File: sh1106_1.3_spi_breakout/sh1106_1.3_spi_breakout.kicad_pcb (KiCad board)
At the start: 2 copper layers, 35 x 31 mm, 20 parts, among them J1 OLED_HEADER, J2 OLED_PANEL, Q1 Q_PMOS_GSD

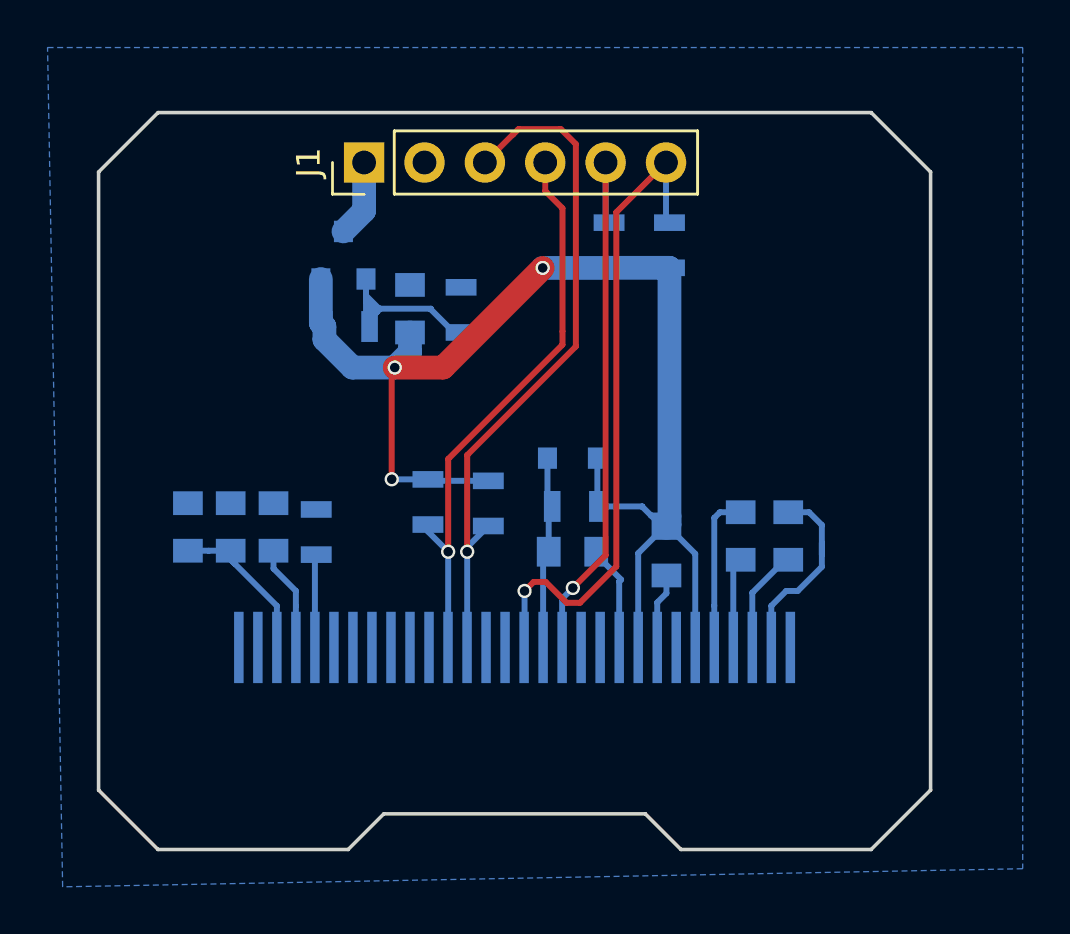
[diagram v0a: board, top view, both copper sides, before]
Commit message: Adjusted dimensions, added silkscreen markings
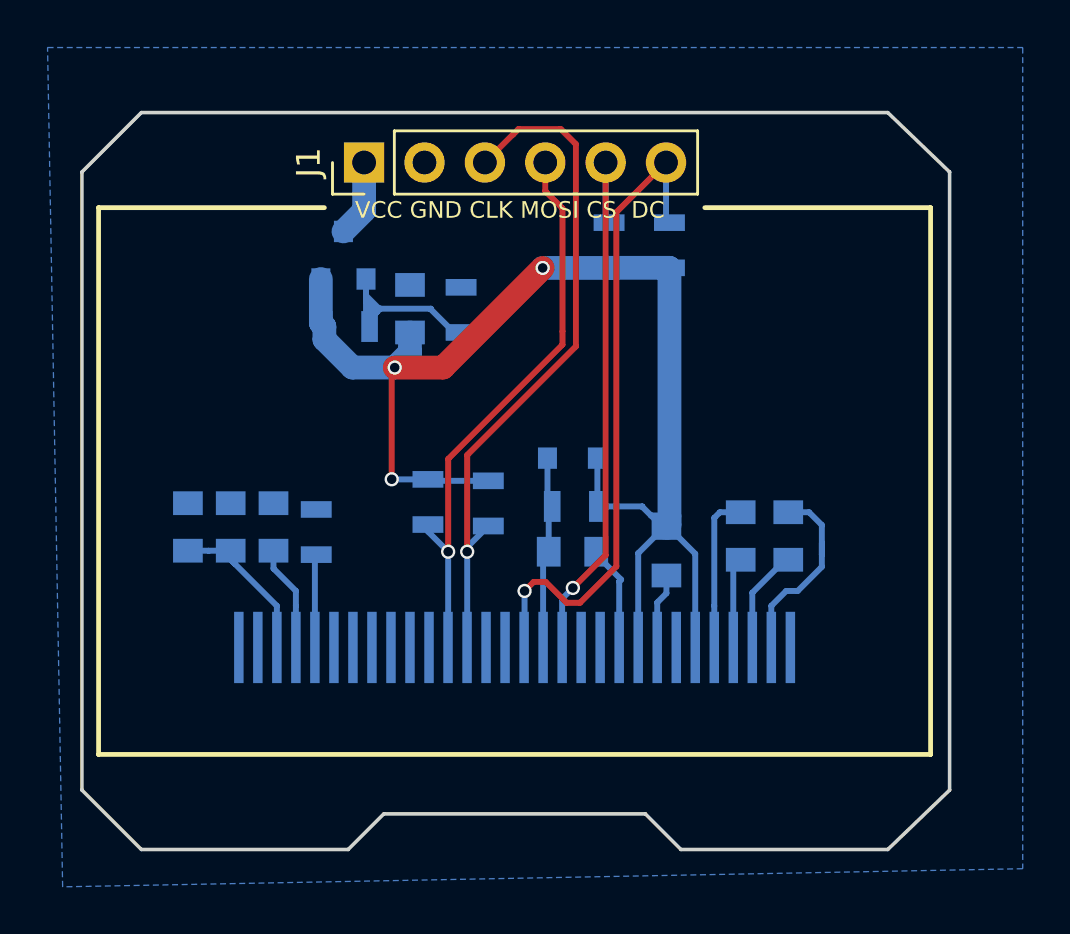
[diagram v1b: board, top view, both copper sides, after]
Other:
- board size 35 x 31 mm -> 36.5 x 31 mm
- board text added: "VCC GND CLK MOSI CS DC"
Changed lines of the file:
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@@
   (general
     (links 57)
-    (no_connects 57)
-    (area 32.424999 19.424999 67.575001 50.575001)
+    (no_connects 15)
+    (area 30.353 16.280952 71.374001 52.070001)
     (thickness 1.6)
-    (drawings 12)
+    (drawings 18)
     (tracks 149)
     (zones 0)
@@
     (pad_to_mask_clearance 0.2)
     (aux_axis_origin 0 0)
-    (visible_elements FFFFFF7F)
+    (visible_elements 7FFFFFFF)
     (pcbplotparams
       (layerselection 0x00030_80000001)
@@
       (zone_connect 1))
   )
+  (gr_text "VCC GND CLK MOSI CS  DC" (at 49.8 23.6) (layer F.SilkS)
+    (effects (font (size 0.7 0.7) (thickness 0.175)))
+  )
+  (gr_line (start 32.5 23.5) (end 42 23.5) (layer F.SilkS) (width 0.2))
+  (gr_line (start 58 23.5) (end 67.5 23.5) (layer F.SilkS) (width 0.2))
+  (gr_line (start 32.5 46.5) (end 32.5 23.5) (layer F.SilkS) (width 0.2))
+  (gr_line (start 67.5 46.5) (end 32.5 46.5) (layer F.SilkS) (width 0.2))
+  (gr_line (start 67.5 23.5) (end 67.5 46.5) (layer F.SilkS) (width 0.2))
   (gr_line (start 44.5 49) (end 43 50.5) (layer Edge.Cuts) (width 0.15))
   (gr_line (start 55.5 49) (end 44.5 49) (layer Edge.Cuts) (width 0.15))
   (gr_line (start 57 50.5) (end 55.5 49) (layer Edge.Cuts) (width 0.15))
-  (gr_line (start 65 50.5) (end 57 50.5) (layer Edge.Cuts) (width 0.15))
-  (gr_line (start 35 50.5) (end 43 50.5) (layer Edge.Cuts) (width 0.15))
-  (gr_line (start 32.5 48) (end 35 50.5) (layer Edge.Cuts) (width 0.15))
-  (gr_line (start 32.5 22) (end 32.5 48) (layer Edge.Cuts) (width 0.15))
-  (gr_line (start 35 19.5) (end 32.5 22) (layer Edge.Cuts) (width 0.15))
-  (gr_line (start 67.5 48) (end 65 50.5) (layer Edge.Cuts) (width 0.15))
-  (gr_line (start 67.5 22) (end 67.5 48) (layer Edge.Cuts) (width 0.15))
-  (gr_line (start 65 19.5) (end 67.5 22) (layer Edge.Cuts) (width 0.15))
-  (gr_line (start 35 19.5) (end 65 19.5) (layer Edge.Cuts) (width 0.15))
+  (gr_line (start 65.7 50.5) (end 57 50.5) (layer Edge.Cuts) (width 0.15))
+  (gr_line (start 34.3 50.5) (end 43 50.5) (layer Edge.Cuts) (width 0.15))
+  (gr_line (start 31.8 48) (end 34.3 50.5) (layer Edge.Cuts) (width 0.15))
+  (gr_line (start 31.8 22) (end 31.8 48) (layer Edge.Cuts) (width 0.15))
+  (gr_line (start 34.3 19.5) (end 31.8 22) (layer Edge.Cuts) (width 0.15))
+  (gr_line (start 68.3 48) (end 65.7 50.5) (layer Edge.Cuts) (width 0.15))
+  (gr_line (start 68.3 22) (end 68.3 48) (layer Edge.Cuts) (width 0.15))
+  (gr_line (start 65.7 19.5) (end 68.3 22) (layer Edge.Cuts) (width 0.15))
+  (gr_line (start 34.3 19.5) (end 65.7 19.5) (layer Edge.Cuts) (width 0.15))
   (segment (start 51.435 37.973) (end 51.435 36.216) (width 0.25) (layer B.Cu) (net 1))
   (segment (start 51.435 36.216) (end 51.583 36.068) (width 0.25) (layer B.Cu) (net 1))

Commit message: Small routing adjustments
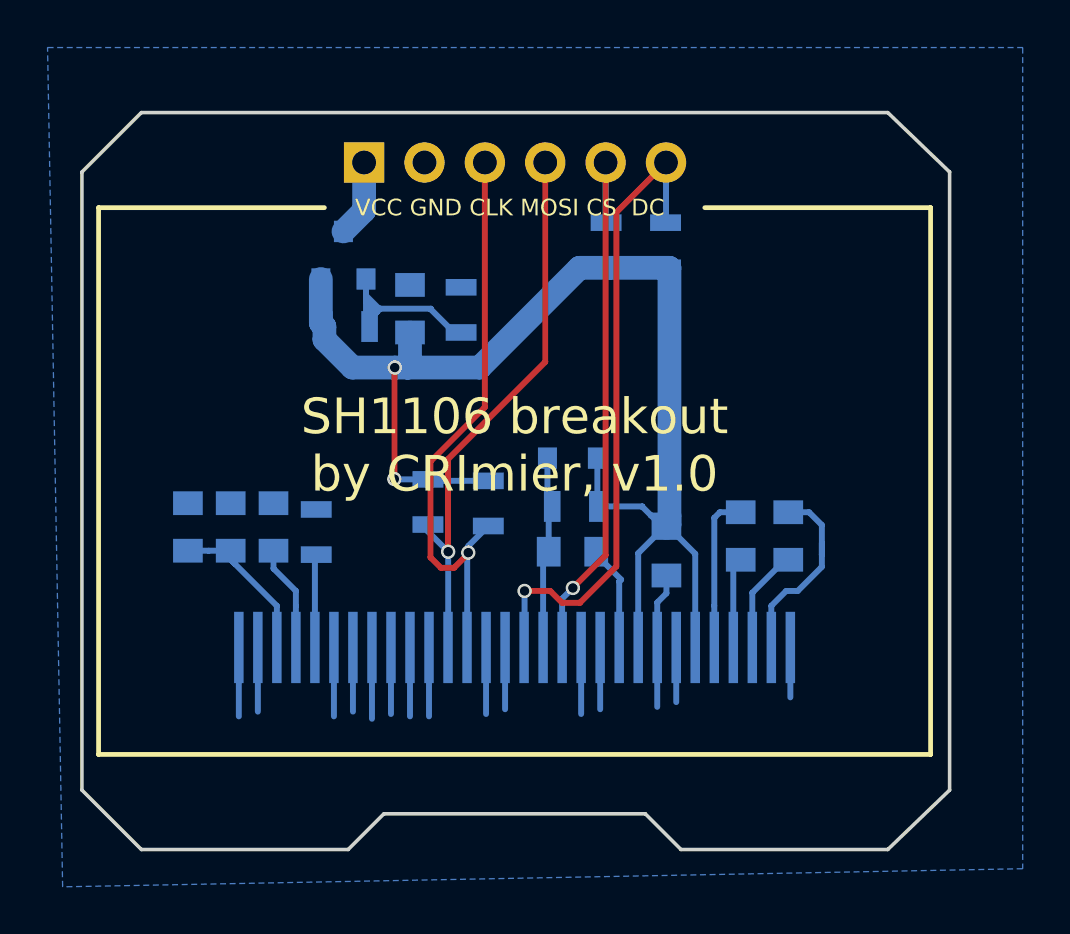
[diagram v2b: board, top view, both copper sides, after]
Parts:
- J1: moved to B.Cu
- moved R1 0.16 mm to (56.4, 25.1)
- moved R4 0.12 mm to (53.9, 25.1)
- turned J1 to 270 degrees
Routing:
- net GND: track 7.68 -> 48.2 mm
- net CLK: track 29.2 -> 25.1 mm
- net MOSI: track 24.2 -> 23.6 mm
- net +3V3: track 58.1 -> 57.6 mm, vias 3 -> 2
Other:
- board text added: "SH1106 breakout by CRImier, v1.0"

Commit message: Fixing the FPC connector on the SH1106 PCB - v1.2
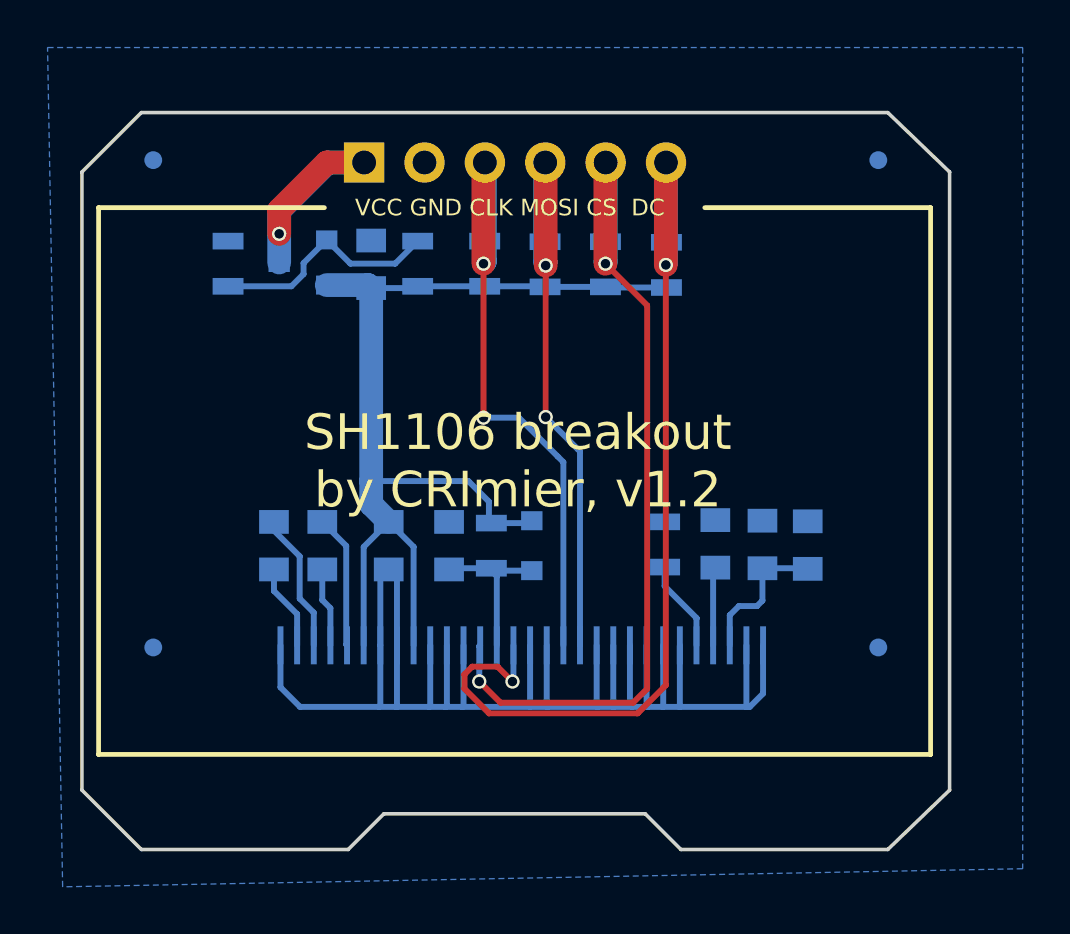
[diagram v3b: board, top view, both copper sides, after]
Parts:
- added FID1: FID, Fiducials:Fiducial_0.75mm_Dia_1.5mm_Outer, B.Cu at (34.8, 21.5)
- added FID2: FID, Fiducials:Fiducial_0.75mm_Dia_1.5mm_Outer, B.Cu at (65.3, 21.5)
- added FID3: FID, Fiducials:Fiducial_0.75mm_Dia_1.5mm_Outer, B.Cu at (34.8, 42.0)
- added FID4: FID, Fiducials:Fiducial_0.75mm_Dia_1.5mm_Outer, B.Cu at (65.3, 42.0)
- C1: value C_Small -> 10uF
- C2, C4, C5, C6, C8: value C_Small -> 1uF
- C3: value C_Small -> 4.7uF
- C7: value C_Small -> 100nF
- D1: value D_Small -> 1N4148
- J2: footprint libs:FPC_30 -> libs:FPC_30_correct
- Q1: value Q_PMOS_GSD -> CJ2305
- R1, R2, R3, R4, R5, R8: value R_Small -> 10K
- R6: value R_Small -> 390K
- R7: value R_Small -> 1K
- moved J2 92.5 mm to (136.7, 74.4)
- moved C4 26.1 mm to (62.3, 37.7)
- moved C5 22.4 mm to (60.4, 37.7)
- moved C2 21.6 mm to (39.9, 37.7), turned to 270 degrees
- moved C3 18.6 mm to (58.4, 37.6)
- moved C6 17.6 mm to (41.9, 37.7)
- moved R6 14.7 mm to (56.3, 37.7)
- moved C7 11.7 mm to (44.7, 37.7)
- moved R3 11.1 mm to (51.3, 25.9), turned to 90 degrees
- moved R2 10.1 mm to (48.7, 25.9), turned to 90 degrees
- moved R7 9.99 mm to (37.9, 25.9)
- moved C1 5.20 mm to (47.2, 37.7), turned to 90 degrees
- moved D1 4.06 mm to (50.7, 37.7), turned to 270 degrees
- moved R8 3.98 mm to (45.9, 25.9), turned to 90 degrees
- moved R5 3.88 mm to (49.0, 37.7), turned to 270 degrees
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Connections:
- D1 pad 1: RESET -> +3V3
- D1 pad 2: +3V3 -> RESET
- J2 pad 12: GND -> MOSI
- J2 pad 13: CS -> CLK
- J2 pad 14: RESET -> GND
- J2 pad 15: DC -> GND
- J2 pad 16: GND -> DC
- J2 pad 17: GND -> RESET
- J2 pad 18: CLK -> CS
- J2 pad 19: MOSI -> GND
- J2 pad 2: Net-(C2-Pad2) -> GND
- J2 pad 22: GND -> +3V3
- J2 pad 25: GND -> +3V3
- J2 pad 26: Net-(J2-Pad26) -> Net-(C6-Pad1)
- J2 pad 27: Net-(C3-Pad1) -> Net-(C6-Pad2)
- J2 pad 28: Net-(C4-Pad1) -> Net-(C2-Pad1)
- J2 pad 29: GND -> Net-(C2-Pad2)
- J2 pad 3: Net-(C2-Pad1) -> Net-(C4-Pad1)
- J2 pad 4: Net-(C6-Pad2) -> Net-(C3-Pad1)
- J2 pad 5: Net-(C6-Pad1) -> Net-(J2-Pad5)
- J2 pad 6: +3V3 -> GND
- J2 pad 9: +3V3 -> GND
- R6 pad 1: Net-(J2-Pad26) -> Net-(J2-Pad5)
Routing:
- net GND: track 48.2 -> 67.8 mm
- net DC: track 27.6 -> 44.5 mm, vias 1 -> 2
- net CS: track 23.8 -> 40.5 mm, vias 1 -> 2
- net +3V3: track 57.6 -> 43.9 mm, vias 2 -> 0
- net VCC: track 3.26 -> 12.0 mm, vias 0 -> 1
- net CLK: track 25.1 -> 31.1 mm, vias 1 -> 2
- net MOSI: track 23.6 -> 29.5 mm, vias 1 -> 2
- net Net-(C2-Pad2): track 8.45 -> 3.59 mm
- net Net-(J2-Pad26): track 3.93 -> 0.00 mm
- net Net-(J2-Pad5): track 0.00 -> 3.85 mm
- net Net-(C2-Pad1): track 4.39 -> 5.88 mm
- net RESET: track 8.41 -> 7.01 mm
- net Net-(C3-Pad1): track 4.46 -> 3.31 mm
- net Net-(C6-Pad1): track 6.66 -> 5.62 mm
- net Net-(C4-Pad1): track 7.07 -> 6.17 mm
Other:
- board text added: "SH1106 breakout by CRImier, v1.2"
- board text removed: "SH1106 breakout by CRImier, v1.0"
